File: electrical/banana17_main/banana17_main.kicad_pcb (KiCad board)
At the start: 2 copper layers, 100 x 100 mm, 66 parts, among them J1 USB_C_Receptacle_USB2.0_16P, SW1 SW, SW10 SW, SW11 SW, SW12 SW, SW13 SW, SW14 SW, SW15 SW, SW16 SW, SW17 SW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

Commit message: Split plane complete.
Split plane complete.
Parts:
- moved C9 1.34 mm to (101.3, 77.8), turned to 180 degrees
- moved C13 0.72 mm to (98.7, 63.5)
- moved C8 0.71 mm to (101.3, 81.0)
- moved C6 0.35 mm to (113.0, 82.4)
- moved C1 0.05 mm to (104.0, 74.3)
- moved C11 0.05 mm to (102.0, 74.3)
- moved C4 0.05 mm to (103.0, 74.3)
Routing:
- net +3V3: track 63.1 -> 28.5 mm, vias 0 -> 17
- net +1V1: track 25.8 -> 9.46 mm, vias 4 -> 2
- net /USB_D-: track 13.3 -> 0.00 mm
- net /USB_D+: track 14.1 -> 2.75 mm
- net /MCU_D+: track 4.07 -> 0.00 mm
- net /MCU_D-: track 4.06 -> 0.00 mm
- net GND: track 34.2 -> 32.7 mm, vias 27 -> 31
- added copper zone on In2.Cu, net +1V1
- added copper zone on In2.Cu, net +3V3
- added copper zone on In1.Cu, net GND
- removed copper zone on F.Cu, net GND
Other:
- copper layers 2 -> 4
- rule pad_to_mask_clearance: 0 -> 0.038

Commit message: Differential pair complete. Gerber files plotted.
Differential pair complete. Gerber files plotted.
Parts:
- moved R2 1.31 mm to (105.4, 71.1)
- moved R1 1.31 mm to (106.5, 71.1)
- moved J1 0.13 mm to (105.5, 52.8)
- moved C10 0.12 mm to (107.4, 73.7)
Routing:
- net /USB_D-: track 0.00 -> 12.8 mm
- net /USB_D+: track 2.75 -> 13.1 mm
- net /MCU_D-: track 0.00 -> 5.39 mm
- net /MCU_D+: track 0.00 -> 5.37 mm
- net +1V1: track 9.46 -> 10.6 mm, vias 2 -> 3
- net +3V3: track 28.5 -> 29.4 mm, vias 17 -> 15
- net COL2: track 222.4 -> 222.9 mm

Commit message: Final changes.
Final changes.
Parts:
- moved R3 0.29 mm to (104.1, 63.0)
- moved J1 0.27 mm to (105.5, 53.0)
- moved R4 0.27 mm to (107.8, 63.3)

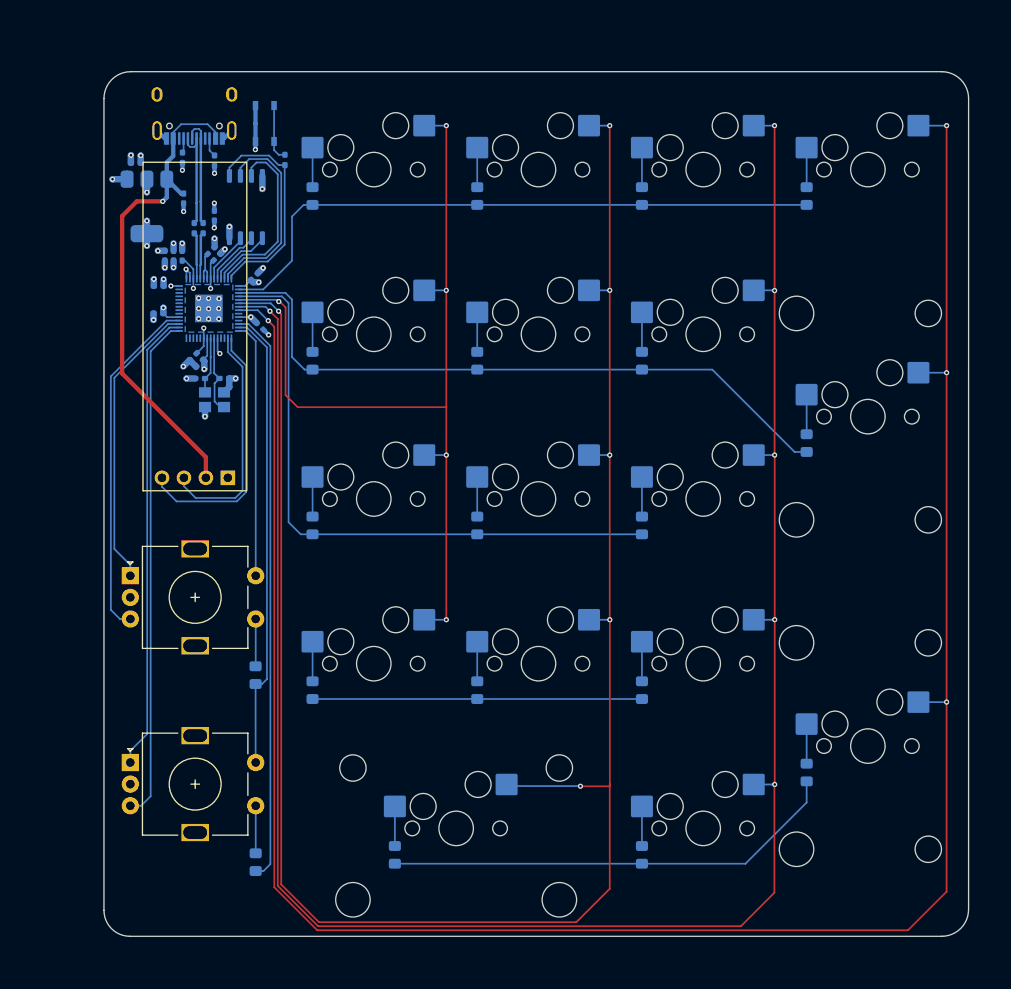
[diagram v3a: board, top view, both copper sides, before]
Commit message: Increased width to accomodate for encoder knobs.
Increased width to accomodate for encoder knobs.
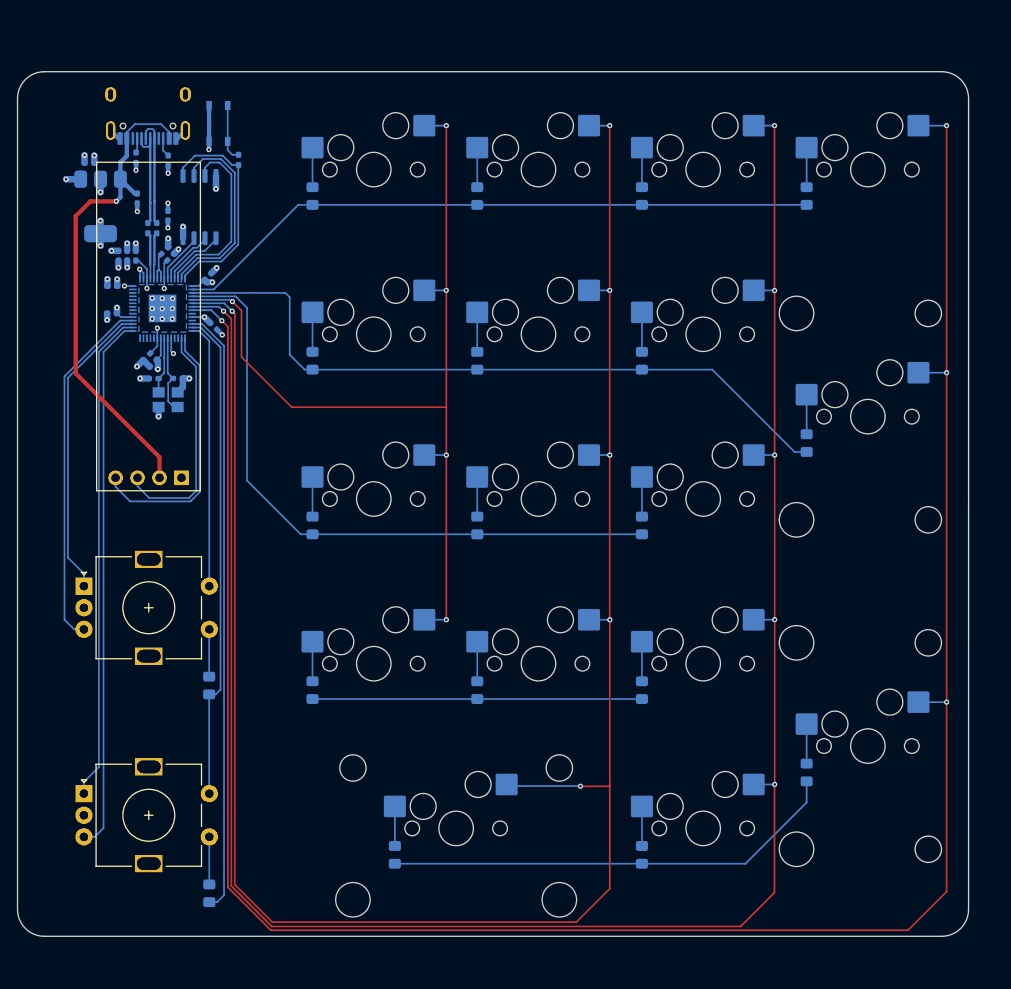
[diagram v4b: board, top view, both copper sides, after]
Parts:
- moved ENC2 6.46 mm to (92.7, 136.5)
- moved ENC_D2 6.46 mm to (107.2, 148.0)
- moved ENC_D1 5.50 mm to (107.2, 124.0)
- moved ENC1 5.50 mm to (92.7, 112.5)
- moved C11 5.37 mm to (96.7, 74.3)
- moved C13 5.37 mm to (93.3, 63.5)
- moved C16 5.37 mm to (100.8, 88.5)
- moved C5 5.37 mm to (107.0, 76.7)
- moved R2 5.37 mm to (100.1, 71.1)
- moved R5 5.37 mm to (110.6, 63.2)
- moved U4 5.37 mm to (106.1, 68.7)
- moved BOOT1 5.37 mm to (108.2, 59.0)
- moved C1 5.37 mm to (98.7, 74.3)
- moved C10 5.37 mm to (102.0, 73.7)
- moved C12 5.37 mm to (98.8, 67.7)
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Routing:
- net COL3: track 232.5 -> 237.9 mm
- net COL2: track 222.9 -> 228.3 mm
- net ROW1: track 77.2 -> 82.6 mm
- net COL4: track 249.8 -> 255.2 mm
- net ROW5: track 53.2 -> 56.8 mm
- net ROW6: track 66.7 -> 70.3 mm
- net ENC2_B: track 58.5 -> 62.1 mm
- net ENC2_A: track 53.3 -> 56.9 mm
- net COL1: track 102.4 -> 105.1 mm
- net ROW0: track 72.7 -> 75.1 mm
- net ROW2: track 72.9 -> 75.1 mm
- net COL0: track 29.6 -> 30.8 mm
- net ENC1_A: track 33.7 -> 34.9 mm
- net ENC1_B: track 40.3 -> 41.4 mm
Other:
- board size 100 x 100 mm -> 110 x 100 mm

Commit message: Reduce PCB size less than 100mm x 100m for cheaper PCB.
Reduce PCB size less than 100mm x 100m for cheaper PCB.
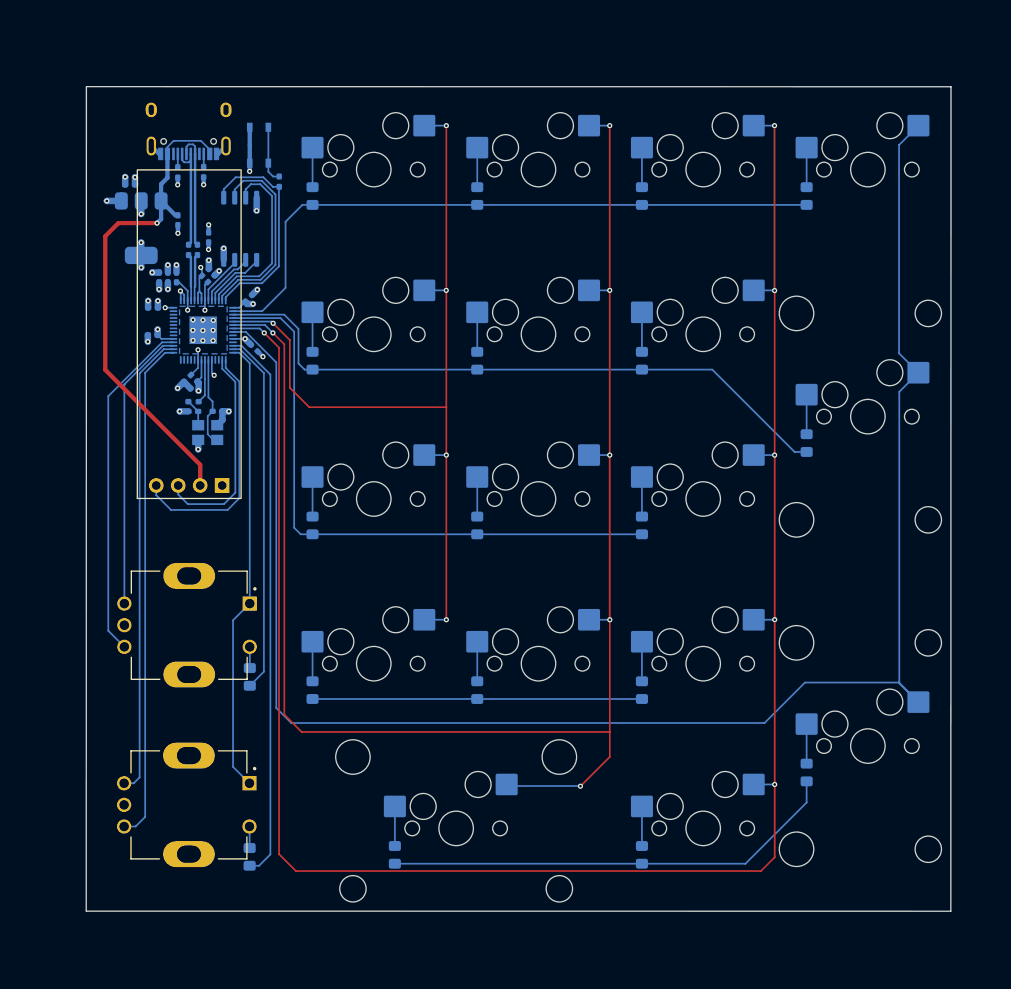
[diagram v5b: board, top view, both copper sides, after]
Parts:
- removed ENC1, ENC2: RotaryEncoder_Switch, Rotary_Encoder:RotaryEncoder_Alps_EC11E-Switch_Vertical_H20mm
- added MT1: PEC11R-4215F-S0024, PEC11R-4215K:XDCR_PEC11R-4215F-S0024, F.Cu at (104.9, 117.0)
- added MT2: PEC11R-4215F-S0024, PEC11R-4215K:XDCR_PEC11R-4215F-S0024, F.Cu at (104.8, 137.8)
- added R6: 1k, Resistor_SMD:R_0402_1005Metric_Pad0.72x0.64mm_HandSolder, B.Cu at (105.4, 91.2)
- SW15: footprint MX_Hotswap:MX-Hotswap-2U -> MX_Hotswap:MX-Hotswap-2U-ReversedStabilizers
- moved ENC_D2 6.29 mm to (111.8, 143.8)
- moved C16 5.95 mm to (105.3, 92.3)
- moved Y1 5.95 mm to (107.0, 94.7)
- moved C15 5.95 mm to (108.1, 92.3)
- moved C9 5.33 mm to (100.7, 80.3)
- moved R2 5.33 mm to (104.8, 73.6)
- moved U2 5.33 mm to (99.3, 71.1)
- moved R5 5.33 mm to (115.3, 65.7)
- moved BOOT1 5.33 mm to (112.9, 61.5)
- moved C1 5.33 mm to (103.4, 76.8)
- moved C10 5.33 mm to (106.7, 76.2)
- moved C11 5.33 mm to (101.4, 76.8)
- moved C12 5.33 mm to (103.5, 70.2)
- moved C13 5.33 mm to (98.0, 66.1)
- moved C14 5.33 mm to (107.1, 72.2)
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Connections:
- C16 pad 2: /XOUT -> Net-(C16-Pad2)
- Y1 pad 3: /XOUT -> Net-(C16-Pad2)
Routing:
- net COL4: track 255.2 -> 194.7 mm, vias 4 -> 0
- net COL2: track 228.3 -> 184.2 mm
- net COL0: track 30.8 -> 52.8 mm
- net COL3: track 237.9 -> 220.4 mm
- net ROW5: track 56.8 -> 41.6 mm
- net ROW1: track 82.6 -> 75.3 mm
- net ROW6: track 70.3 -> 64.2 mm
- net COL1: track 105.1 -> 99.5 mm
- net ROW2: track 75.1 -> 70.9 mm
- net ENC2_B: track 62.1 -> 58.5 mm
- net Net-(C16-Pad2): track 0.00 -> 3.20 mm
- net ENC2_A: track 56.9 -> 53.9 mm
- net Net-(ENC_D1-A): track 5.47 -> 2.46 mm
- net Net-(ENC_D2-A): track 5.50 -> 2.50 mm
- net OLED_SCL: track 27.0 -> 24.6 mm
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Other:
- board size 110 x 100 mm -> 100 x 95.4 mm
- board text added: "BY G.K.C"

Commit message: Rerouting matrix.
Rerouting matrix.
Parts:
- moved R5 1.76 mm to (114.0, 64.5)
- moved BOOT1 1.25 mm to (112.9, 60.2)
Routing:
- net COL3: track 220.4 -> 162.5 mm, vias 6 -> 5
- net COL2: track 184.2 -> 150.0 mm, vias 6 -> 5
- net ROW2: track 70.9 -> 38.1 mm
- net ROW0: track 75.9 -> 57.1 mm
- net COL4: track 194.7 -> 179.0 mm, vias 0 -> 3
- net ROW1: track 75.3 -> 61.1 mm
- net COL1: track 99.5 -> 101.3 mm, vias 5 -> 4
- net /~{USB_BOOT}: track 6.63 -> 5.75 mm
- net GND: track 32.6 -> 33.1 mm
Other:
- outline, holes or cut-outs redrawn

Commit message: Additional changes to routing.
Additional changes to routing.
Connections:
- U1 pad 11: /GPIO8 -> ROW4
- U1 pad 13: ROW5 -> /GPIO10
- U1 pad 2: ROW0 -> COL4
- U1 pad 3: ROW1 -> COL3
- U1 pad 4: ROW2 -> COL2
- U1 pad 6: COL2 -> ROW0
- U1 pad 7: COL3 -> ROW1
- U1 pad 8: COL4 -> ROW2
- U1 pad 9: /GPIO7 -> ROW3
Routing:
- net ROW2: track 38.1 -> 67.8 mm
- net ROW0: track 57.1 -> 77.3 mm
- net COL1: track 101.3 -> 114.6 mm, vias 4 -> 5
- net COL2: track 150.0 -> 162.3 mm, vias 5 -> 6
- net COL3: track 162.5 -> 173.8 mm, vias 5 -> 6
- net ROW1: track 61.1 -> 72.3 mm
- net COL4: track 179.0 -> 181.0 mm, vias 3 -> 4

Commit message: Tracks rerouted.
Tracks rerouted.
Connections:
- U1 pad 11: ROW4 -> /GPIO8
- U1 pad 12: ROW6 -> /GPIO9
- U1 pad 13: /GPIO10 -> ROW3
- U1 pad 14: COL0 -> ROW4
- U1 pad 15: OLED_SDA -> /GPIO12
- U1 pad 16: OLED_SCL -> ROW6
- U1 pad 17: /GPIO14 -> ROW5
- U1 pad 18: /GPIO15 -> COL0
- U1 pad 27: /GPIO16 -> OLED_SDA
- U1 pad 28: /GPIO17 -> OLED_SCL
- U1 pad 9: ROW3 -> /GPIO7
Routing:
- net ROW4: track 53.0 -> 126.5 mm
- net ROW3: track 38.1 -> 83.6 mm
- net OLED_SDA: track 28.7 -> 15.9 mm
- net OLED_SCL: track 24.6 -> 22.0 mm
- net ROW6: track 64.1 -> 61.5 mm
- net ROW5: track 41.6 -> 40.5 mm
- net COL0: track 52.8 -> 52.0 mm
